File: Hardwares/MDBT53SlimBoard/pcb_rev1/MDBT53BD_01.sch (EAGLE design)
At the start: 33 parts, among them CN1 IF_6PIN, CN2 USB4105-GF-A, U1 RV-3028-C7, U2 XC6206P302MR-G

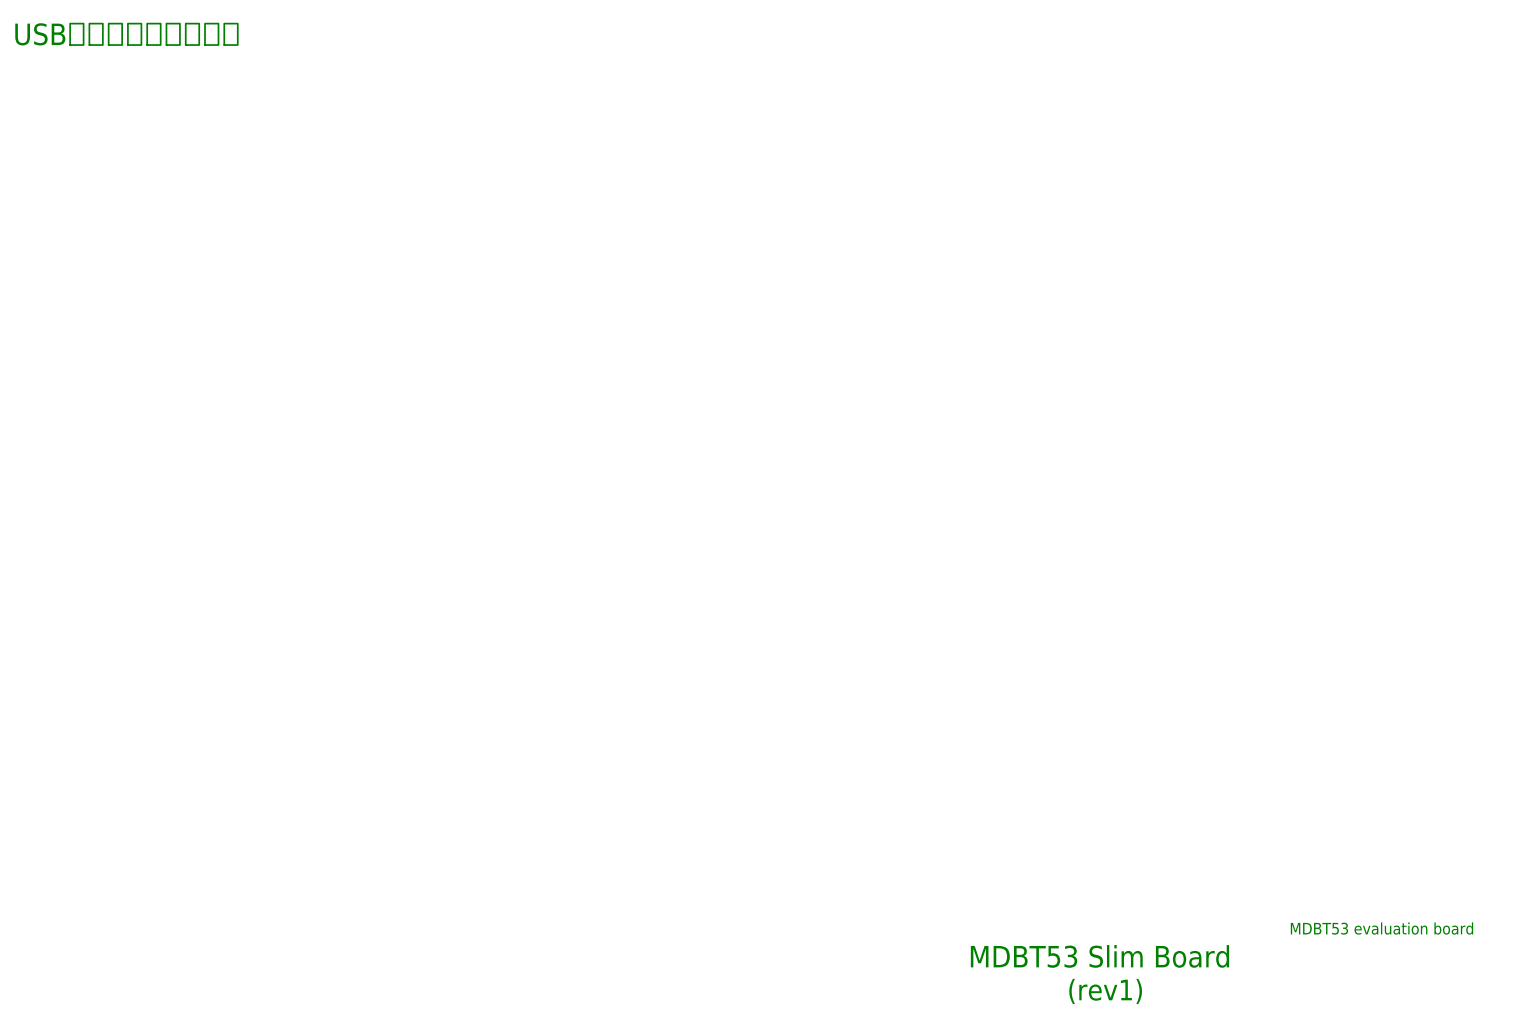
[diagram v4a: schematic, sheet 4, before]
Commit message: 回路図の作成
・TFTインターフェース部を追加
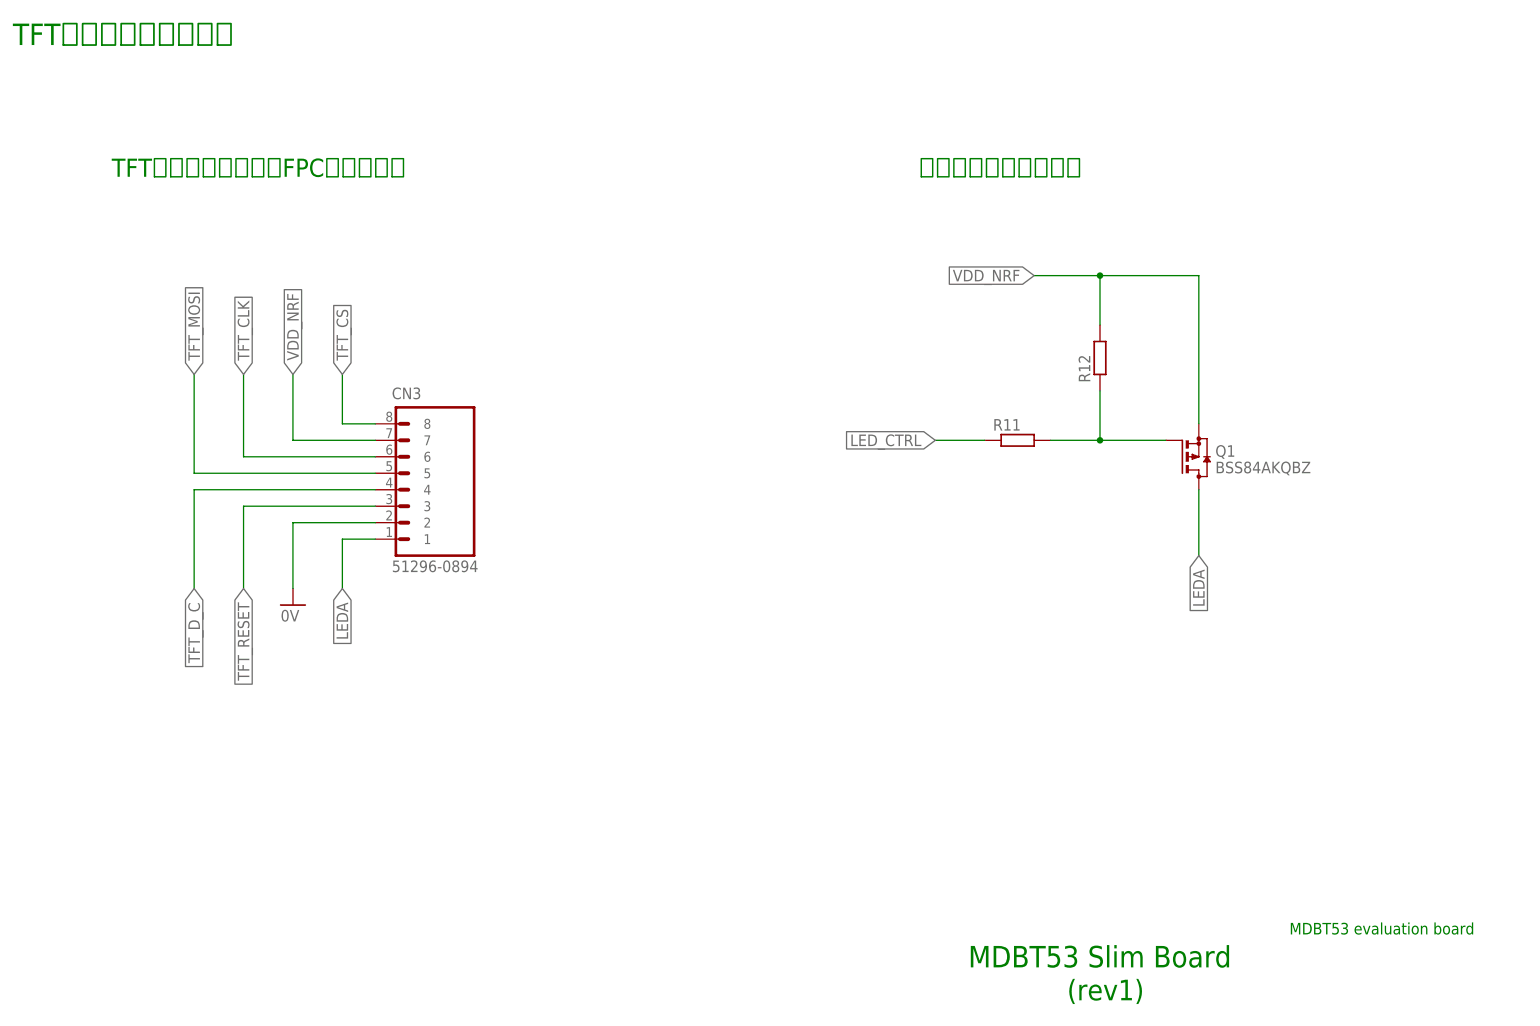
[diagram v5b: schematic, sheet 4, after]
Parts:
- added CN3: 51296-0894, Connectors:51296-0894
- added Q1: BSS84AKQBZ, Parts:BSS84AKQBZ
- added R11, R12: (no value), Parts:RESISTOR_0402N
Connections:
- new net LEDA: CN3.1, Q1.D
- new net LED_CTRL: R11.1
- new net N$14: Q1.G, R11.2, R12.1
- new net TFT_CLK: CN3.6
- new net TFT_CS: CN3.8
- new net TFT_D_C: CN3.4
- new net TFT_MOSI: CN3.5
- new net TFT_RESET: CN3.3
- net 0V: now also CN3.2
- net VDD_NRF: now also CN3.7, Q1.S, R12.2
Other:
- note added: "TFTインターフェース部"
- note added: "TFTモジュール接続用FPCコネクター"
- note added: "バックライト制御回路"
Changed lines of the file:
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@@
 <part name="GND11" library="Supply" deviceset="0V" device=""/>
 <part name="GND12" library="Supply" deviceset="0V" device=""/>
+<part name="CN3" library="Connectors" deviceset="51296-0894" device=""/>
+<part name="GND13" library="Supply" deviceset="0V" device=""/>
+<part name="R11" library="Parts" deviceset="RESISTOR" device="_0402N"/>
+<part name="R12" library="Parts" deviceset="RESISTOR" device="_0402N"/>
+<part name="Q1" library="Parts" deviceset="BSS84AKQB" device="Z"/>
 </parts>
 <sheets>
@@
 <text x="182.88" y="10.16" size="3.175" layer="91">(rev1)</text>
 <text x="217.17" y="20.32" size="1.778" layer="91">MDBT53 evaluation board</text>
-<text x="20.32" y="157.48" size="3.302" layer="91">USBインターフェース部</text>
+<text x="20.32" y="157.48" size="3.302" layer="91">TFTインターフェース部</text>
+<text x="35.56" y="137.16" size="2.794" layer="91">TFTモジュール接続用FPCコネクター</text>
+<text x="160.02" y="137.16" size="2.794" layer="91">バックライト制御回路</text>
 </plain>
 <instances>
 <instance part="FRAME4" gate="G$1" x="0" y="0"/>
+<instance part="CN3" gate="G$1" x="76.2" y="96.52"/>
+<instance part="GND13" gate="1" x="63.5" y="71.12"/>
+<instance part="R11" gate="G$1" x="170.18" y="96.52"/>
+<instance part="R12" gate="G$1" x="187.96" y="104.14" rot="R90"/>
+<instance part="Q1" gate="G$1" x="203.2" y="93.98"/>
 </instances>
 <busses>
 </busses>
 <nets>
+<net name="VDD_NRF" class="0">
+<segment>
+<pinref part="Q1" gate="G$1" pin="S"/>
+<wire x1="177.8" y1="121.92" x2="187.96" y2="121.92" width="0.1524" layer="91"/>
+<wire x1="187.96" y1="121.92" x2="203.2" y2="121.92" width="0.1524" layer="91"/>
+<wire x1="203.2" y1="121.92" x2="203.2" y2="99.06" width="0.1524" layer="91"/>
+<pinref part="R12" gate="G$1" pin="2"/>
+<wire x1="187.96" y1="121.92" x2="187.96" y2="114.3" width="0.1524" layer="91"/>
+<label x="177.8" y="121.92" size="1.778" layer="95" rot="R180" xref="yes"/>
+<junction x="187.96" y="121.92"/>
+</segment>
+<segment>
+<pinref part="CN3" gate="G$1" pin="7"/>
+<wire x1="76.2" y1="96.52" x2="63.5" y2="96.52" width="0.1524" layer="91"/>
+<wire x1="63.5" y1="96.52" x2="63.5" y2="106.68" width="0.1524" layer="91"/>
+<label x="63.5" y="106.68" size="1.778" layer="95" rot="R90" xref="yes"/>
+</segment>
+</net>
+<net name="N$14" class="0">
+<segment>
+<pinref part="R12" gate="G$1" pin="1"/>
+<wire x1="187.96" y1="104.14" x2="187.96" y2="96.52" width="0.1524" layer="91"/>
+<pinref part="Q1" gate="G$1" pin="G"/>
+<wire x1="187.96" y1="96.52" x2="198.12" y2="96.52" width="0.1524" layer="91"/>
+<pinref part="R11" gate="G$1" pin="2"/>
+<wire x1="180.34" y1="96.52" x2="187.96" y2="96.52" width="0.1524" layer="91"/>
+<junction x="187.96" y="96.52"/>
+</segment>
+</net>
+<net name="LED_CTRL" class="0">
+<segment>
+<pinref part="R11" gate="G$1" pin="1"/>
+<wire x1="170.18" y1="96.52" x2="162.56" y2="96.52" width="0.1524" layer="91"/>
+<label x="162.56" y="96.52" size="1.778" layer="95" rot="R180" xref="yes"/>
+</segment>
+</net>
+<net name="LEDA" class="0">
+<segment>
+<pinref part="Q1" gate="G$1" pin="D"/>
+<wire x1="203.2" y1="88.9" x2="203.2" y2="78.74" width="0.1524" layer="91"/>
+<label x="203.2" y="78.74" size="1.778" layer="95" rot="R270" xref="yes"/>
+</segment>
+<segment>
+<pinref part="CN3" gate="G$1" pin="1"/>
+<wire x1="76.2" y1="81.28" x2="71.12" y2="81.28" width="0.1524" layer="91"/>
+<wire x1="71.12" y1="81.28" x2="71.12" y2="73.66" width="0.1524" layer="91"/>
+<label x="71.12" y="73.66" size="1.778" layer="95" rot="R270" xref="yes"/>
+</segment>
+</net>
+<net name="0V" class="0">
+<segment>
+<pinref part="CN3" gate="G$1" pin="2"/>
+<pinref part="GND13" gate="1" pin="0V"/>
+<wire x1="76.2" y1="83.82" x2="63.5" y2="83.82" width="0.1524" layer="91"/>
+<wire x1="63.5" y1="83.82" x2="63.5" y2="73.66" width="0.1524" layer="91"/>
+</segment>
+</net>
+<net name="TFT_RESET" class="0">
+<segment>
+<pinref part="CN3" gate="G$1" pin="3"/>
+<wire x1="76.2" y1="86.36" x2="55.88" y2="86.36" width="0.1524" layer="91"/>
+<wire x1="55.88" y1="86.36" x2="55.88" y2="73.66" width="0.1524" layer="91"/>
+<label x="55.88" y="73.66" size="1.778" layer="95" rot="R270" xref="yes"/>
+</segment>
+</net>
+<net name="TFT_D_C" class="0">
+<segment>
+<pinref part="CN3" gate="G$1" pin="4"/>
+<wire x1="76.2" y1="88.9" x2="48.26" y2="88.9" width="0.1524" layer="91"/>
+<wire x1="48.26" y1="88.9" x2="48.26" y2="73.66" width="0.1524" layer="91"/>
+<label x="48.26" y="73.66" size="1.778" layer="95" rot="R270" xref="yes"/>
+</segment>
+</net>
+<net name="TFT_MOSI" class="0">
+<segment>
+<pinref part="CN3" gate="G$1" pin="5"/>
+<wire x1="76.2" y1="91.44" x2="48.26" y2="91.44" width="0.1524" layer="91"/>
+<wire x1="48.26" y1="91.44" x2="48.26" y2="106.68" width="0.1524" layer="91"/>
+<label x="48.26" y="106.68" size="1.778" layer="95" rot="R90" xref="yes"/>
+</segment>
+</net>
+<net name="TFT_CLK" class="0">
+<segment>
+<pinref part="CN3" gate="G$1" pin="6"/>
+<wire x1="76.2" y1="93.98" x2="55.88" y2="93.98" width="0.1524" layer="91"/>
+<wire x1="55.88" y1="93.98" x2="55.88" y2="106.68" width="0.1524" layer="91"/>
+<label x="55.88" y="106.68" size="1.778" layer="95" rot="R90" xref="yes"/>
+</segment>
+</net>
+<net name="TFT_CS" class="0">
+<segment>
+<pinref part="CN3" gate="G$1" pin="8"/>
+<wire x1="76.2" y1="99.06" x2="71.12" y2="99.06" width="0.1524" layer="91"/>
+<wire x1="71.12" y1="99.06" x2="71.12" y2="106.68" width="0.1524" layer="91"/>
+<label x="71.12" y="106.68" size="1.778" layer="95" rot="R90" xref="yes"/>
+</segment>
+</net>
 </nets>
 </sheet>
